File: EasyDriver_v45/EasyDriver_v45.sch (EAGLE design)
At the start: 43 parts, among them IC1 A3967SLB, IC2 V_REG_317SMD

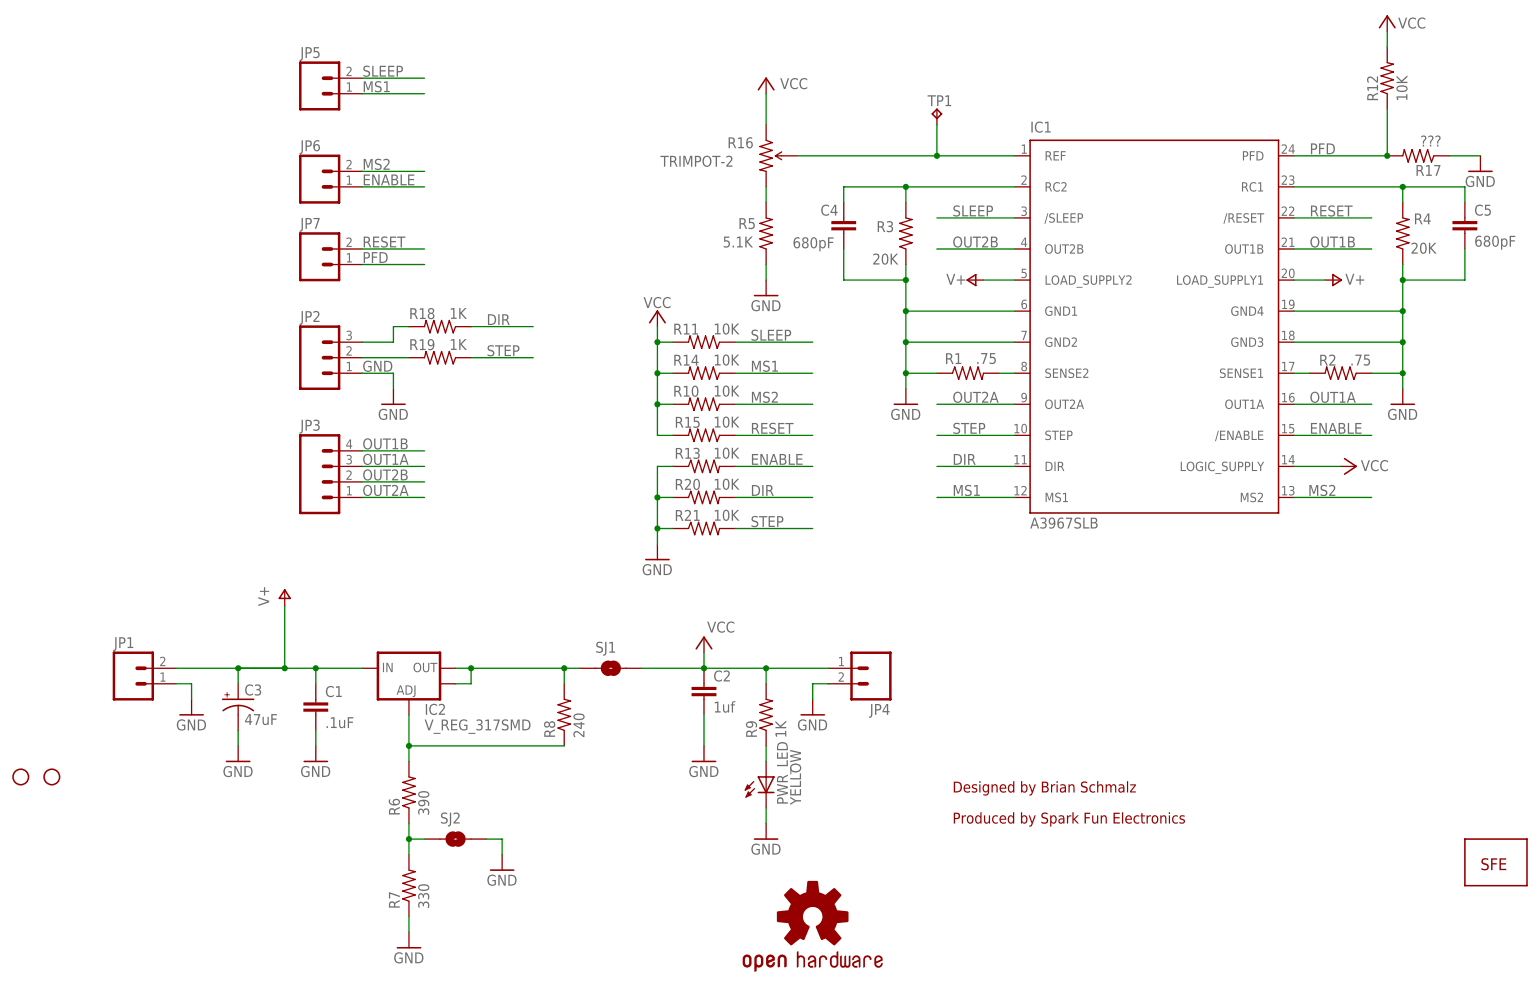
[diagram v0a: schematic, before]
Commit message: Version 4.5 updates -
* All Rs and Cs are now normal 0603 SparkFun footprints
* Added series Rs and pull downs for STEP and DIR inputs
* Updated pot footprint to TRIMPOT-3MM-2 for better soldering
* Switched license from CC BY 3.0 to CC BY-SA 3.0
* Fixed pot direction silk screen
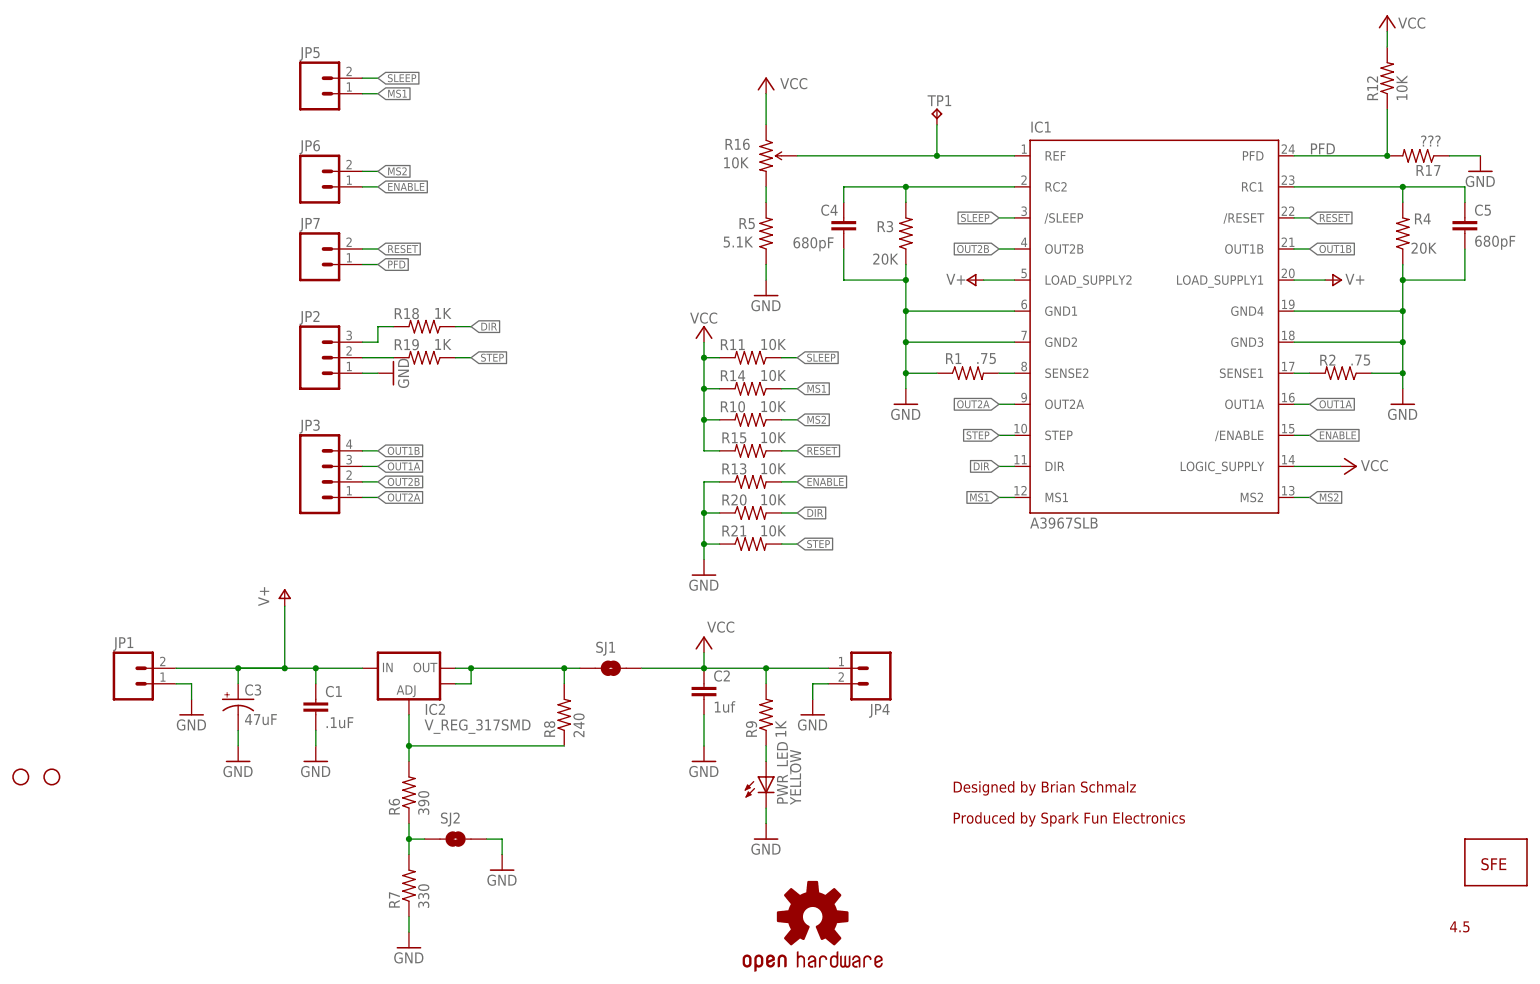
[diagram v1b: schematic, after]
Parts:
- R16: value TRIMPOT-2 -> 10K; device SparkFun-Electromechanical:TRIMPOT-2 -> SparkFun-Electromechanical:TRIMPOT3MM-2
- R20, R21: device SparkFun03_30_09:RESISTOR0402 -> SparkFun-Resistors:RESISTOR0603
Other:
- note added: "4.5"
- note added: "Added series resistors and pull downs on STEP/DIR Updated pot fooprint Made bottom layer GND rather than VCC Updated to latest SparkFun footprints Swithed from CC BY 3.0 to CC BY-SA 3.0 license Fixed pot silkscreen direction"
- note added: "Attribution Share Alike (CC BY-SA) 3.0 US License"
- note added: "v4.3 12/09/09 BPS Added mounting holes"
- note added: "v4.4 1/3/12 BPS : C3 now 47uF"
- note added: "v4.4 10/24/20 BPS"
- note added: "v4.5 2/25/14 BPS"
- note removed: "Added series resistors and pull downs on STEP/DIR Updated pot fooprint Made bottom layer GND rather than VCC Updated to latest SparkFun footprints"
- note removed: "Attribution 3.0 US License"
- note removed: "C3 now at 47uF"
- note removed: "v4.3 (12/09/2009)"
- note removed: "v4.3 Added mounting holes"
- note removed: "v4.4 (1/3/2012)"
- note removed: "v4.4 (10/24/2010)"
- note removed: "v4.5 (2/25/2014)"
- moved on the sheet: R10, R11, R13, R14, R15, R18, R19, R20, R21

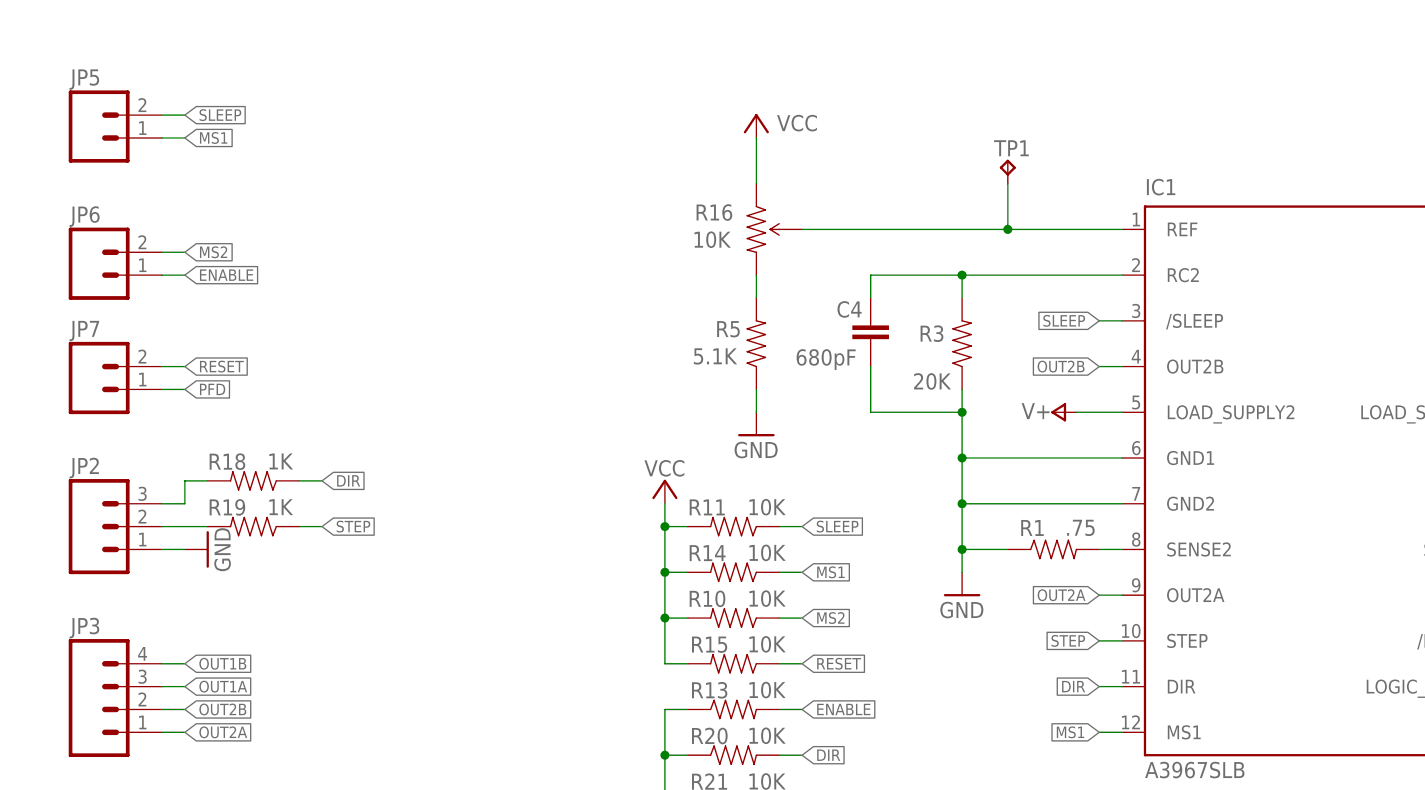
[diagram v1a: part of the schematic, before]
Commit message: Small updates to schematic and board
* Rotated ground symbol on schematic so it matched other ground symbols
* Changed TP1 to standard SparkFun test point footprint
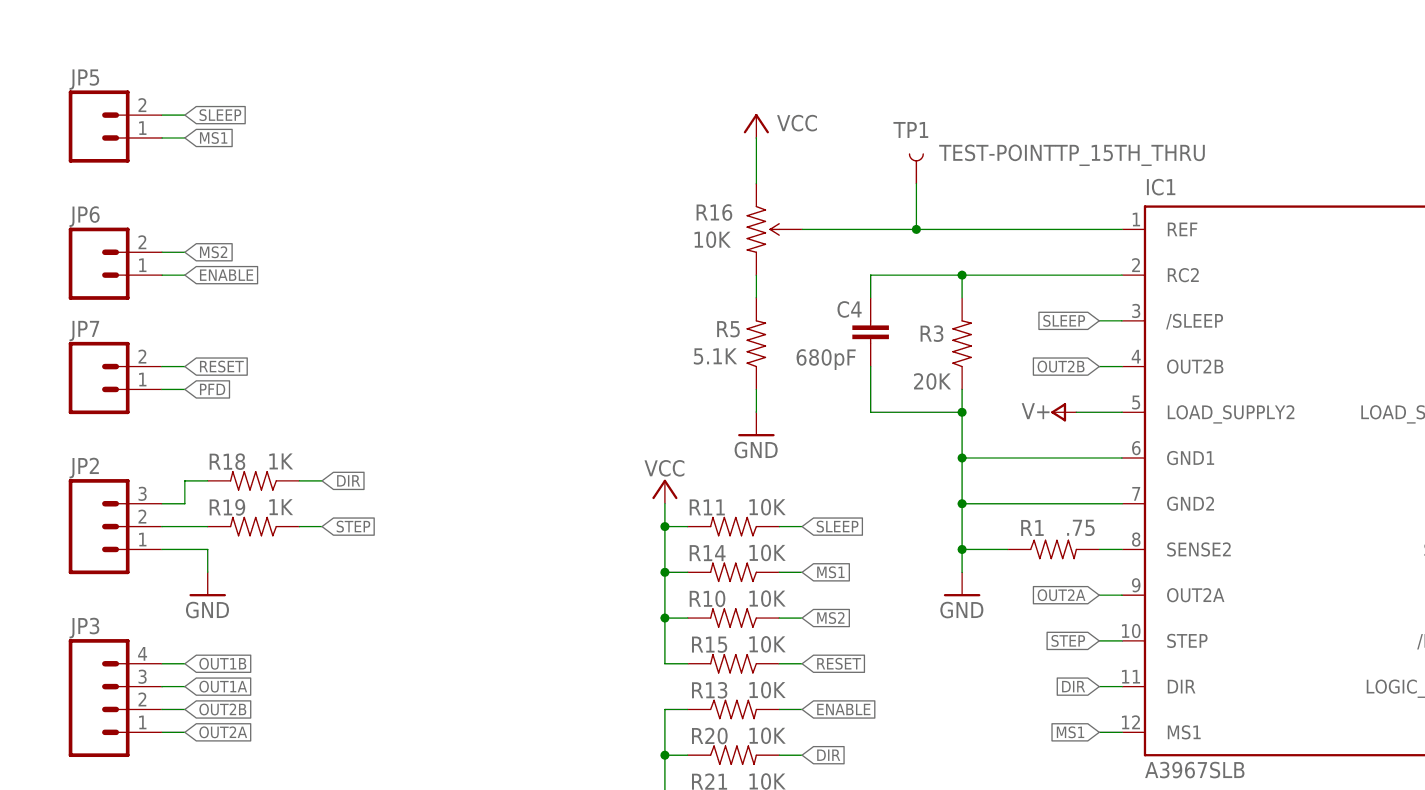
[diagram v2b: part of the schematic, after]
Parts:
- TP1: value TPPAD1-13 -> TEST-POINTTP_15TH_THRU; device testpad:TPPAD1-13 -> SparkFun-Passives:TEST-POINTTP_15TH_THRU
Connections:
- net N$12: now also TP1.1; no longer TP1.TP
